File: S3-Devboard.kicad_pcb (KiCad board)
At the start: 2 copper layers, 4 parts, among them U1 ESP32-S3(R8), X1 TX322540M4FBCE2T

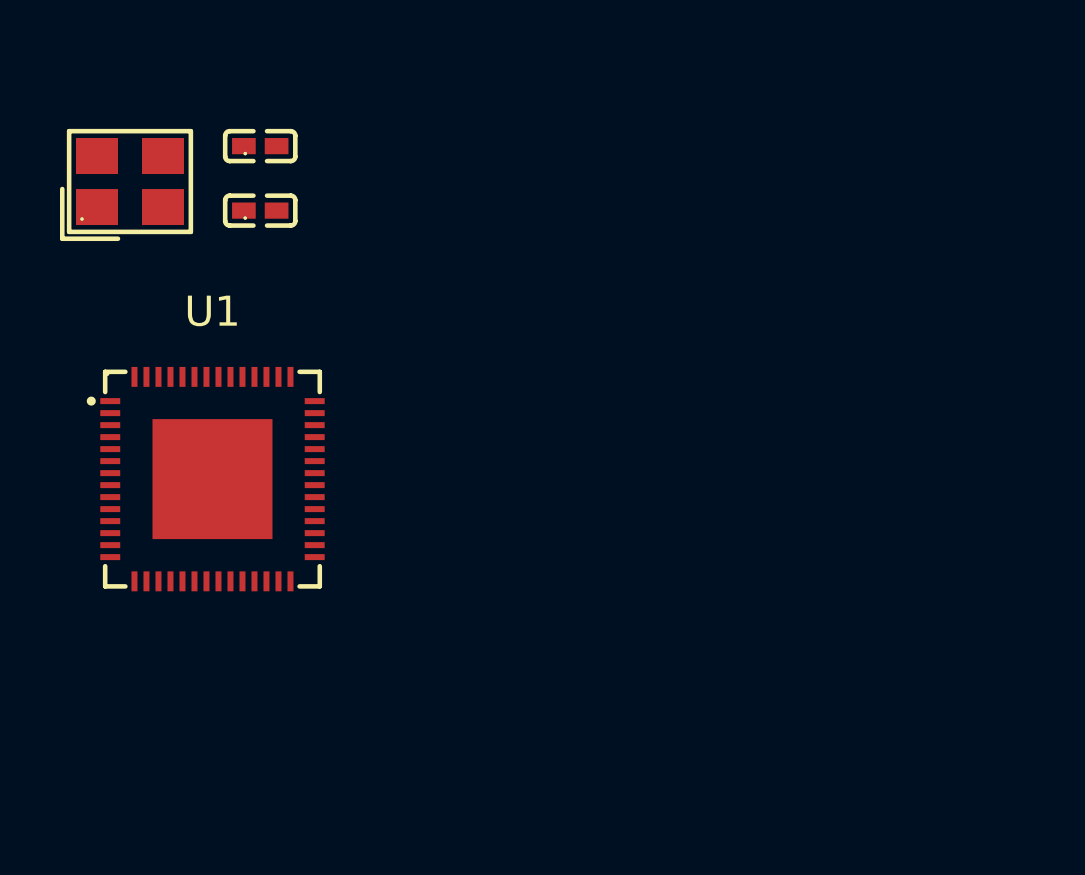
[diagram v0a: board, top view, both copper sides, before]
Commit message: Updated pins
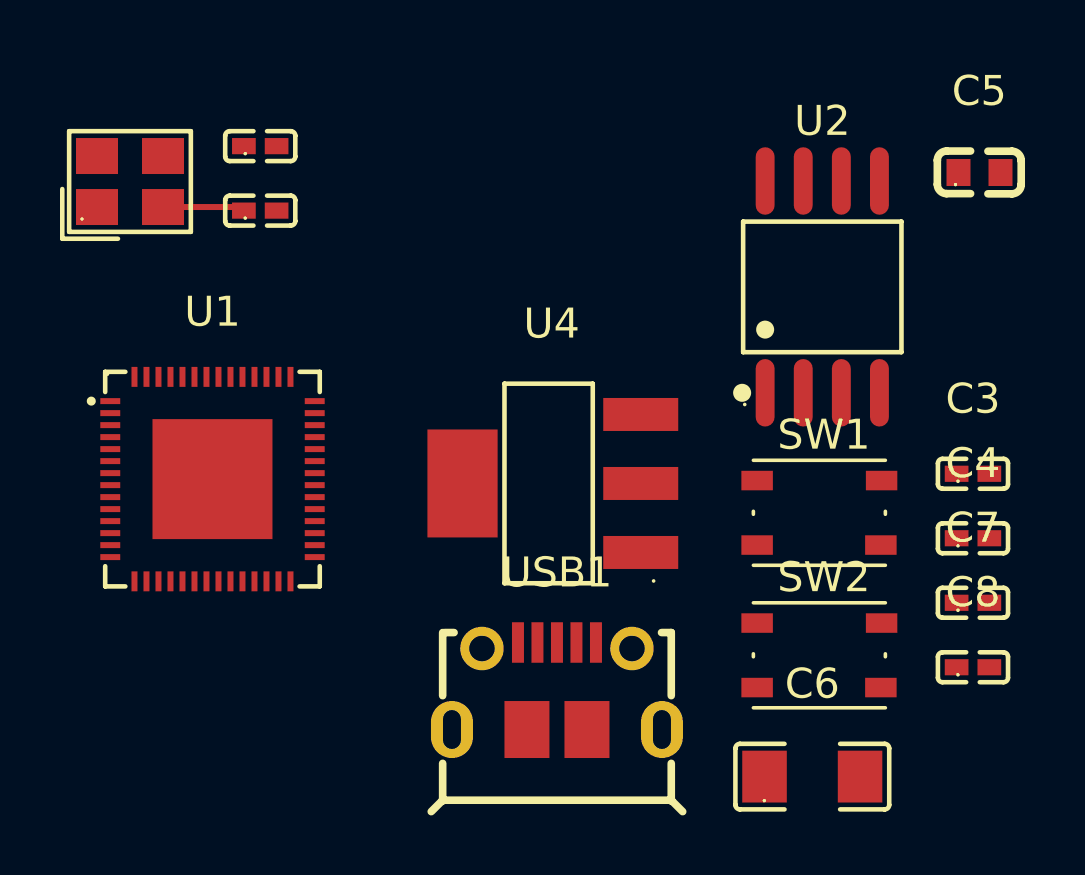
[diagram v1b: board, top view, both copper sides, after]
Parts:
- added C3: 10u, jlc_footprints:C0402, F.Cu at (140.1, 79.9)
- added C4: 100n, jlc_footprints:C0402, F.Cu at (140.1, 82.0)
- added C5: 22u, jlc_footprints:C0603, F.Cu at (140.3, 69.8)
- added C6: 100u, jlc_footprints:C1206, F.Cu at (134.7, 90.0)
- added C7: 100n, jlc_footprints:C0402, F.Cu at (140.1, 84.2)
- added C8: 1u, jlc_footprints:C0402, F.Cu at (140.1, 86.3)
- added SW1: IO0, Button_Switch_SMD:SW_Push_1P1T_NO_Vertical_Wuerth_434133025816, F.Cu at (134.9, 81.2)
- added SW2: RST, Button_Switch_SMD:SW_Push_1P1T_NO_Vertical_Wuerth_434133025816, F.Cu at (134.9, 85.9)
- added U2: W25Q128JVSIQTR, jlc_footprints:SOIC-8_L5.3-W5.3-P1.27-LS8.0-BL, F.Cu at (135.0, 73.7)
- added U4: AMS1117, jlc_footprints:SOT-223-3_L6.5-W3.4-P2.30-LS7.0-BR, F.Cu at (126.0, 80.2)
- added USB1: 1050171001, jlc_footprints:MICRO-USB-SMD_1050171001, F.Cu at (126.2, 87.0)
- X1: value TX322540M4FBCE2T -> 40MHz
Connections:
- U1 pad 10: unconnected-(U1-GPIO5-Pad10) -> IO5
- U1 pad 11: unconnected-(U1-GPIO6-Pad11) -> IO6
- U1 pad 12: unconnected-(U1-GPIO7-Pad12) -> IO7
- U1 pad 13: unconnected-(U1-GPIO8-Pad13) -> IO8
- U1 pad 14: unconnected-(U1-GPIO9-Pad14) -> IO9
- U1 pad 15: unconnected-(U1-GPIO10-Pad15) -> IO10
- U1 pad 16: unconnected-(U1-GPIO11-Pad16) -> IO11
- U1 pad 17: unconnected-(U1-GPIO12-Pad17) -> IO12
- U1 pad 18: unconnected-(U1-GPIO13-Pad18) -> IO13
- U1 pad 19: unconnected-(U1-GPIO14-Pad19) -> IO14
- U1 pad 21: unconnected-(U1-XTAL_32K_P-Pad21) -> IO15
- U1 pad 22: unconnected-(U1-XTAL_32K_N-Pad22) -> IO16
- U1 pad 23: unconnected-(U1-GPIO17-Pad23) -> IO17
- U1 pad 24: unconnected-(U1-GPIO18-Pad24) -> IO18
- U1 pad 25: unconnected-(U1-GPIO19-Pad25) -> USB_N
- U1 pad 26: unconnected-(U1-GPIO20-Pad26) -> USB_P
- U1 pad 27: unconnected-(U1-GPIO21-Pad27) -> IO21
- U1 pad 29: unconnected-(U1-VDD_SPI-Pad29) -> +3V3
- U1 pad 30: unconnected-(U1-SPIHD-Pad30) -> SD_HD
- U1 pad 31: unconnected-(U1-SPIWP-Pad31) -> SD_WP
- U1 pad 32: unconnected-(U1-SPICS0-Pad32) -> SD_CS0
- U1 pad 33: unconnected-(U1-SPICLK-Pad33) -> SD_CLK
- U1 pad 34: unconnected-(U1-SPIQ-Pad34) -> SD_IQ
- U1 pad 35: unconnected-(U1-SPID-Pad35) -> SD_ID
- U1 pad 36: unconnected-(U1-SPICLK_N-Pad36) -> IO48
- U1 pad 37: unconnected-(U1-SPICLK_P-Pad37) -> IO47
- U1 pad 38: unconnected-(U1-GPIO33-Pad38) -> IO33
- U1 pad 39: unconnected-(U1-GPIO34-Pad39) -> IO34
- U1 pad 40: unconnected-(U1-GPIO35-Pad40) -> IO35
- U1 pad 41: unconnected-(U1-GPIO36-Pad41) -> IO36
- U1 pad 42: unconnected-(U1-GPIO37-Pad42) -> IO37
- U1 pad 43: unconnected-(U1-GPIO38-Pad43) -> IO38
- U1 pad 44: unconnected-(U1-MTCK-Pad44) -> IO39
- U1 pad 45: unconnected-(U1-MTDO-Pad45) -> IO40
- U1 pad 47: unconnected-(U1-MTDI-Pad47) -> IO41
- U1 pad 48: unconnected-(U1-MTMS-Pad48) -> IO42
- U1 pad 5: unconnected-(U1-GPIO0-Pad5) -> IO0
- U1 pad 51: unconnected-(U1-GPIO45-Pad51) -> IO45
- U1 pad 52: unconnected-(U1-GPIO46-Pad52) -> IO46
- U1 pad 6: unconnected-(U1-GPIO1-Pad6) -> IO1
- U1 pad 7: unconnected-(U1-GPIO2-Pad7) -> IO2
- U1 pad 8: unconnected-(U1-GPIO3-Pad8) -> IO3
- U1 pad 9: unconnected-(U1-GPIO4-Pad9) -> IO4
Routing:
- net GND: track 0.00 -> 2.75 mm

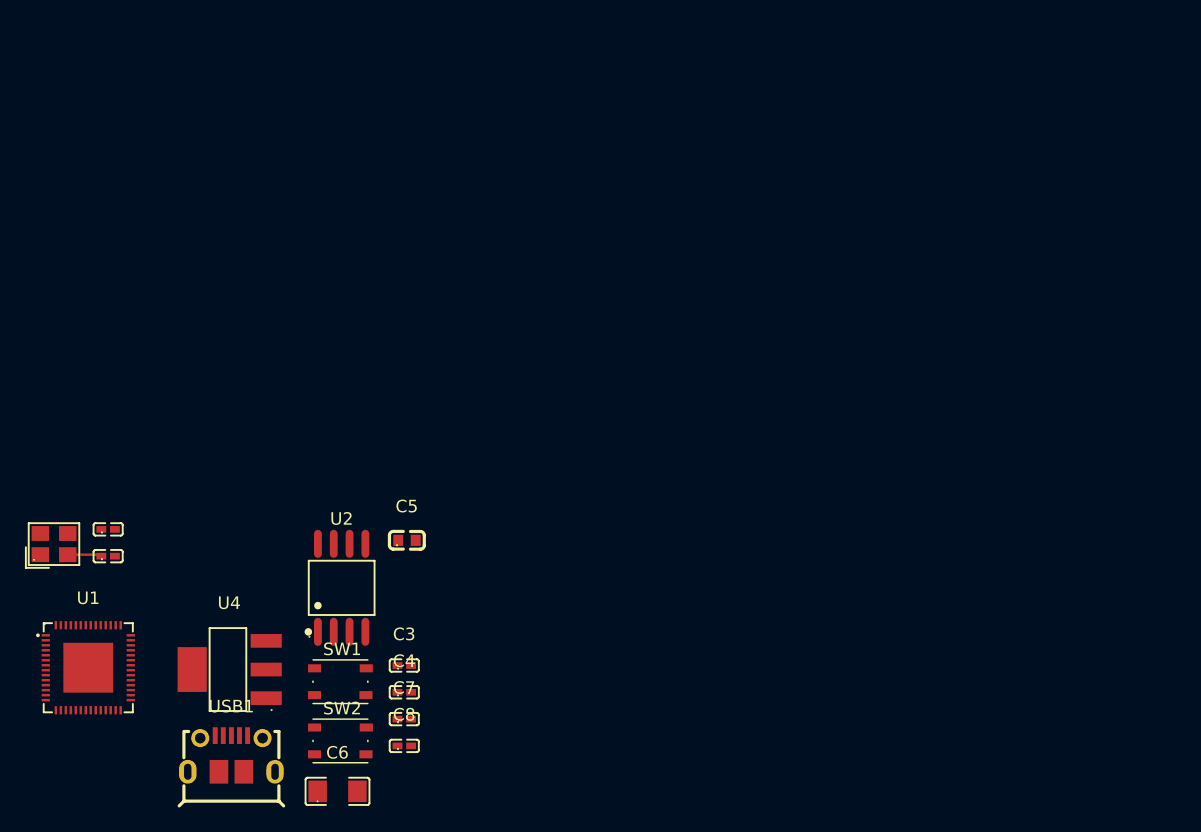
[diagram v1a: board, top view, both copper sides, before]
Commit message: Changes
- Add caps for SPI Flash
- Add reset circuit
- Add net classes
- Add VSPI rather than constant 3V3
- Add Schottky diode for the power delivery
- Add PCB Antenna
- Add provisional headers
- Break out the GPIOs to Vias
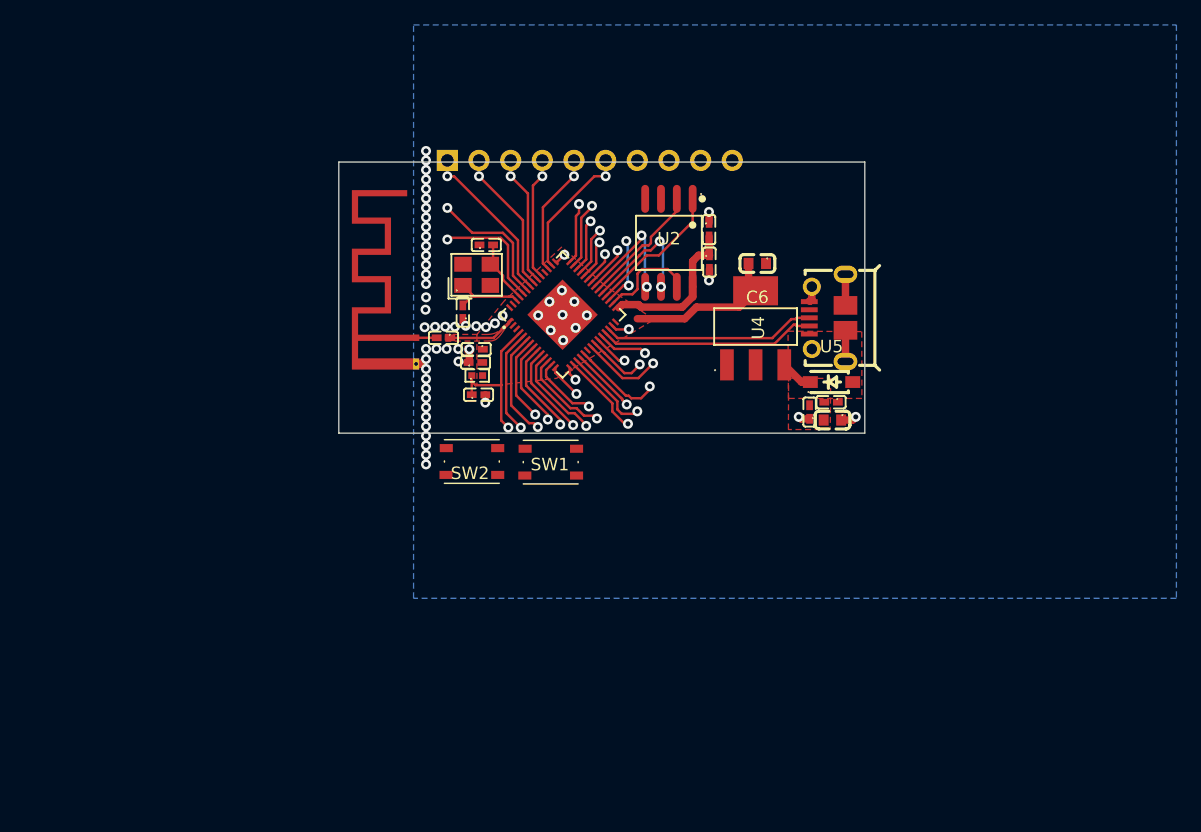
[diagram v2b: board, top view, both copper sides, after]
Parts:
- added C10: 1u, jlc_footprints:C0402, F.Cu at (145.8, 54.5)
- added C11: 1u, jlc_footprints:C0402, F.Cu at (146.0, 58.2)
- added C12: 0402CG5R6C500NT, jlc_footprints:C0402, F.Cu at (143.2, 53.6)
- added C9: 100n, jlc_footprints:C0402, F.Cu at (145.8, 55.6)
- added E1: Antenna_Trace, RF_Antenna:Texas_SWRA117D_2.4GHz_Right, F.Cu at (141.0, 53.6)
- added R1: 10k, jlc_footprints:R0402, F.Cu at (145.9, 56.6)
- added REF**: PinHeader_1x10_P2.54mm_Vertical, Connector_PinHeader_2.54mm:PinHeader_1x10_P2.54mm_Vertical, B.Cu at (143.5, 39.4)
- added U5: B5819W_C8598, jlc_footprints:SOD-123_L2.7-W1.6-LS3.7-RD-1, F.Cu at (174.3, 57.1)
- C6: value 100u -> 22u; footprint jlc_footprints:C1206 -> jlc_footprints:C0603
- moved USB1 59.2 mm to (174.0, 52.0), turned to 90 degrees
- moved C6 54.1 mm to (168.4, 47.6), turned to 180 degrees
- moved U4 50.3 mm to (168.2, 52.8), turned to -90 degrees
- moved U1 47.4 mm to (152.8, 51.8), turned to 45 degrees
- moved C7 46.3 mm to (164.5, 44.9), turned to -90 degrees
- moved C8 45.9 mm to (164.5, 47.5), turned to -90 degrees
- moved C4 41.4 mm to (174.3, 58.8), turned to 180 degrees
- moved X1 40.2 mm to (145.9, 48.5)
- moved C2 39.3 mm to (146.6, 46.1)
- moved C3 38.4 mm to (172.6, 59.6), turned to 90 degrees
- moved U2 38.2 mm to (161.3, 46.0), turned to 180 degrees
- moved C5 35.5 mm to (174.4, 60.2), turned to 180 degrees
- moved C1 33.4 mm to (144.8, 51.5), turned to 90 degrees
- moved SW2 24.8 mm to (145.5, 63.5), turned to 180 degrees
- moved SW1 24.4 mm to (151.8, 63.6), turned to 180 degrees
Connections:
- C7 pad 2: +3V3 -> V_SPI
- C8 pad 1: +3V3 -> V_SPI
- SW1 pad 2: GPIO0 -> IO0
- U1 pad 1: unconnected-(U1-LNA_IN-Pad1) -> LNA
- U1 pad 2: unconnected-(U1-VDD3P3-Pad2) -> +3V3
- U1 pad 20: unconnected-(U1-VDD3P3_RTC-Pad20) -> +3V3
- U1 pad 29: +3V3 -> V_SPI
- U1 pad 3: unconnected-(U1-VDD3P3-Pad3) -> +3V3
- U1 pad 4: unconnected-(U1-CHIP_PU-Pad4) -> RESET
- U1 pad 46: unconnected-(U1-VDD3P3_CPU-Pad46) -> +3V3
- U1 pad 55: unconnected-(U1-VDDA-Pad55) -> +3V3
- U1 pad 56: unconnected-(U1-VDDA-Pad56) -> +3V3
- U1 pad 57: unconnected-(U1-GND-Pad57) -> GND
- U2 pad 8: +3V3 -> V_SPI
- USB1 pad 1: unconnected-(USB1-VBUS-Pad1) -> VBUS
- USB1 pad 10: unconnected-(USB1-EP-Pad10) -> GND
- USB1 pad 11: unconnected-(USB1-EP-Pad11) -> GND
- USB1 pad 5: unconnected-(USB1-GND-Pad5) -> GND
- USB1 pad 6: unconnected-(USB1-EP-Pad6) -> GND
- USB1 pad 7: unconnected-(USB1-EP-Pad7) -> GND
- USB1 pad 8: unconnected-(USB1-EP-Pad8) -> GND
- USB1 pad 9: unconnected-(USB1-EP-Pad9) -> GND
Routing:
- net USB_N: track 0.00 -> 17.4 mm
- net USB_P: track 0.00 -> 17.1 mm
- net +3V3: track 0.00 -> 12.8 mm
- net RESET: track 0.00 -> 12.5 mm, vias 0 -> 1
- net V_SPI: track 0.00 -> 12.4 mm
- net unconnected-(U1-U0RXD-Pad50): track 0.00 -> 11.9 mm, vias 0 -> 1
- net SD_CS0: track 0.00 -> 11.4 mm
- net GND: track 2.75 -> 13.9 mm, vias 0 -> 58
- net IO45: track 0.00 -> 10.7 mm, vias 0 -> 1
- net unconnected-(U1-U0TXD-Pad49): track 0.00 -> 10.4 mm, vias 0 -> 1
- net SD_CLK: track 0.00 -> 10.2 mm, vias 0 -> 2
- net SD_IQ: track 0.00 -> 10.2 mm
- net SD_ID: track 0.00 -> 10.1 mm, vias 0 -> 2
- net IO39: track 0.00 -> 9.73 mm, vias 0 -> 1
- net IO46: track 0.00 -> 9.58 mm, vias 0 -> 1
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- added copper zone on F.Cu, net +3V3
- added copper zone on F.Cu, net +5V
- added copper zone on B.Cu, net GND
- added copper zone on F.Cu, net LNA
- added copper zone on F.Cu, net VBUS
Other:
- board outline added: 42.2 x 21.8 mm
